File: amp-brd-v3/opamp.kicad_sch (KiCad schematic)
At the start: 21 parts, among them U2 INA233, U4 LMR36510ADDA

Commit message: Tested DAC and INA, doing new boards
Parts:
- added R8, R9: 10k, Resistor_SMD:R_0402_1005Metric, symbol Device:R
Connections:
- net SCL: now also R9.1
- net SDA: now also R8.1
- net V_{BUS}: now also R8.2, R9.2
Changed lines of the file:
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@@
+	)
+	(junction
+		(at 242.57 106.68)
+		(diameter 0)
+		(color 0 0 0 0)
+	)
+	(junction
+		(at 245.11 109.22)
+		(diameter 0)
+		(color 0 0 0 0)
 	)
 	(junction
@@
 	)
 	(junction
+		(at 242.57 81.28)
+		(diameter 0)
+		(color 0 0 0 0)
+	)
+	(junction
 		(at 57.15 147.32)
 		(diameter 0)
@@
 	(wire
 		(pts
+			(xy 245.11 95.25) (xy 245.11 109.22)
+		)
+		(stroke
+			(width 0)
+			(type default)
+		)
+	)
+	(wire
+		(pts
 			(xy 97.79 135.89) (xy 100.33 135.89)
 		)
@@
 	(wire
 		(pts
+			(xy 245.11 109.22) (xy 250.19 109.22)
+		)
+		(stroke
+			(width 0)
+			(type default)
+		)
+	)
+	(wire
+		(pts
 			(xy 45.72 134.62) (xy 45.72 147.32)
 		)
@@
 	(wire
 		(pts
+			(xy 242.57 81.28) (xy 245.11 81.28)
+		)
+		(stroke
+			(width 0)
+			(type default)
+		)
+	)
+	(wire
+		(pts
 			(xy 139.7 118.11) (xy 130.81 118.11)
 		)
@@
 	(wire
 		(pts
+			(xy 242.57 81.28) (xy 242.57 87.63)
+		)
+		(stroke
+			(width 0)
+			(type default)
+		)
+	)
+	(wire
+		(pts
+			(xy 245.11 81.28) (xy 245.11 87.63)
+		)
+		(stroke
+			(width 0)
+			(type default)
+		)
+	)
+	(wire
+		(pts
 			(xy 209.55 67.31) (xy 215.9 67.31)
 		)
@@
 	(wire
 		(pts
+			(xy 242.57 106.68) (xy 250.19 106.68)
+		)
+		(stroke
+			(width 0)
+			(type default)
+		)
+	)
+	(wire
+		(pts
+			(xy 242.57 95.25) (xy 242.57 106.68)
+		)
+		(stroke
+			(width 0)
+			(type default)
+		)
+	)
+	(wire
+		(pts
 			(xy 83.82 125.73) (xy 96.52 125.73)
 		)
@@
 	(wire
 		(pts
-			(xy 226.06 109.22) (xy 250.19 109.22)
+			(xy 226.06 109.22) (xy 245.11 109.22)
 		)
 		(stroke
@@
 	(wire
 		(pts
-			(xy 226.06 106.68) (xy 250.19 106.68)
+			(xy 226.06 106.68) (xy 242.57 106.68)
 		)
 		(stroke
@@
 		(pts
 			(xy 119.38 118.11) (xy 119.38 120.65)
+		)
+		(stroke
+			(width 0)
+			(type default)
+		)
+	)
+	(wire
+		(pts
+			(xy 237.49 81.28) (xy 242.57 81.28)
 		)
 		(stroke
@@
 		(shape input)
 		(at 85.09 135.89 180)
+		(effects
+			(font
+				(size 1.27 1.27)
+			)
+			(justify right)
+		)
+	)
+	(hierarchical_label "V_{BUS}"
+		(shape input)
+		(at 237.49 81.28 180)
 		(effects
 			(font
@@
 	)
 	(symbol
+		(lib_id "Device:R")
+		(at 242.57 91.44 180)
+		(unit 1)
+		(exclude_from_sim no)
+		(in_bom yes)
+		(on_board yes)
+		(dnp no)
+		(property "Reference" "R8"
+			(at 238.506 90.17 0)
+			(effects
+				(font
+					(size 1.27 1.27)
+				)
+				(justify right)
+			)
+		)
+		(property "Value" "10k"
+			(at 242.57 93.218 90)
+			(effects
+				(font
+					(size 1.27 1.27)
+				)
+				(justify right)
+			)
+		)
+		(property "Footprint" "Resistor_SMD:R_0402_1005Metric"
+			(at 244.348 91.44 90)
+			(effects
+				(font
+					(size 1.27 1.27)
+				)
+				(hide yes)
+			)
+		)
+		(property "Datasheet" "~"
+			(at 242.57 91.44 0)
+			(effects
+				(font
+					(size 1.27 1.27)
+				)
+				(hide yes)
+			)
+		)
+		(property "Description" "Resistor"
+			(at 242.57 91.44 0)
+			(effects
+				(font
+					(size 1.27 1.27)
+				)
+				(hide yes)
+			)
+		)
+		(pin "2"
+		)
+		(pin "1"
+		)
+		(instances
+			(project "amplifier-brd"
+				(path "/4a199ccc-be1f-4132-9551-a46e36599bcb/f2b7aa34-9911-40d3-beee-632deab3d3cc"
+					(reference "R8")
+					(unit 1)
+				)
+			)
+		)
+	)
+	(symbol
 		(lib_id "Device:C")
 		(at 34.29 130.81 0)
@@
 					(unit 1)
 				)
+			)
+		)
+	)
+	(symbol
+		(lib_id "Device:R")
+		(at 245.11 91.44 180)
+		(unit 1)
+		(exclude_from_sim no)
+		(in_bom yes)
+		(on_board yes)
+		(dnp no)
+		(property "Reference" "R9"
+			(at 246.634 90.17 0)
+			(effects
+				(font
+					(size 1.27 1.27)
+				)
+				(justify right)
+			)
+		)
+		(property "Value" "10k"
+			(at 245.11 93.218 90)
+			(effects
+				(font
+					(size 1.27 1.27)
+				)
+				(justify right)
+			)
+		)
+		(property "Footprint" "Resistor_SMD:R_0402_1005Metric"
+			(at 246.888 91.44 90)
+			(effects
+				(font
+					(size 1.27 1.27)
+				)
+				(hide yes)
+			)
+		)
+		(property "Datasheet" "~"
+			(at 245.11 91.44 0)
+			(effects
+				(font
+					(size 1.27 1.27)
+				)
+				(hide yes)
+			)
+		)
+		(property "Description" "Resistor"
+			(at 245.11 91.44 0)
+			(effects
+				(font
+					(size 1.27 1.27)
+				)
+				(hide yes)
+			)
+		)
+		(pin "2"
+		)
+		(pin "1"
+		)
+		(instances
+			(project "amplifier-brd"
+				(path "/4a199ccc-be1f-4132-9551-a46e36599bcb/f2b7aa34-9911-40d3-beee-632deab3d3cc"
+					(reference "R9")
+					(unit 1)
+				)

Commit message: Updated all boards for production
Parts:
- R3: value 10k -> 100k
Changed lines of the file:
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@@
 		)
 	)
-	(text_box "V_{OUT} = -A V_{CTRL} + (1 + A) V_{FB}\nA = R1 / R2\n\nV_{FB} = 1 V\nV_{OUT,absmin} = 1 V\nV_{OUT,absmax} = 28V\n\nR1 = 100k\nR2 = 4.02k\nA = 24.8756\n\nV_{OUT,max} = 25.8756 V\nV_{IN,absmin} = V_{OUT,max} / 0.95 = 27.24 V\nV_{CTRL,min} = 0 ==> V_{OUT} = V_{OUT,max} = 25.8765 V\n\nR_{LOAD} = 20 Ohm\nV_{CTRL,max} = 1.0 V  ==> V_{OUT} = V_{OUT,absmin} = 1.0 V, P_{OUT,absmin} = 0.05 W\nV_{CTRL,max} = 0.96 V ==> V_{OUT} = 2 V, P_{OUT} = 0.2 W\n"
+	(text_box "V_{OUT} = -A V_{CTRL} + (1 + A) V_{FB}\nA = R1 / R2\n\nV_{FB} = 1 V\nV_{OUT,absmin} = 1 V\nV_{OUT,absmax} = 28V\n\nR1 = 100k\nR2 = 4.02k\nA = 24.8756\n\nV_{OUT,max} = 25.8756 V\nV_{IN,absmin} = V_{OUT,max} / 0.95 = 27.24 V\nV_{CTRL,min} = 0 ==> V_{OUT} = V_{OUT,max} = 25.8765 V\n\nR_{LOAD} = 20 Ohm\nV_{CTRL,max} = 1.0 V  ==> V_{OUT} = V_{OUT,absmin} = 1.0 V, P_{OUT,absmin} = 0.05 W\nV_{CTRL,max} = 0.96 V ==> V_{OUT} = 2 V, P_{OUT} = 0.2 W\n\nCTRL_{IN} = High-Z => V_{FB} = 1V = V_{OUT} * 104k / 204k => V_{OUT} = 204 V / 104 ~ 1.96 V\n"
 		(exclude_from_sim no)
 		(at 13.97 13.97 0)
@@
 		(on_board yes)
 		(dnp no)
-		(fields_autoplaced yes)
 		(property "Reference" "R3"
-			(at 115.57 138.43 90)
-			(effects
-				(font
-					(size 1.27 1.27)
-				)
-			)
-		)
-		(property "Value" "10k"
-			(at 115.57 140.97 90)
-			(effects
-				(font
+			(at 120.904 144.78 90)
+			(effects
+				(font
+					(size 1.27 1.27)
+				)
+			)
+		)
+		(property "Value" "100k"
+			(at 115.57 144.78 90)
+			(effects
+				(font

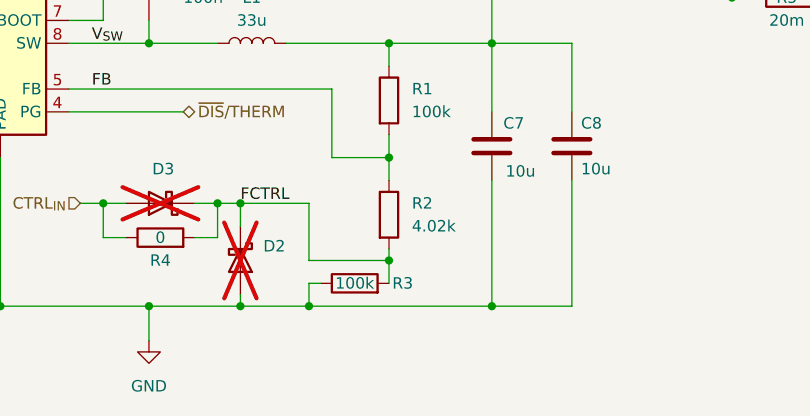
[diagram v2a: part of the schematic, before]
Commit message: Added part numbers
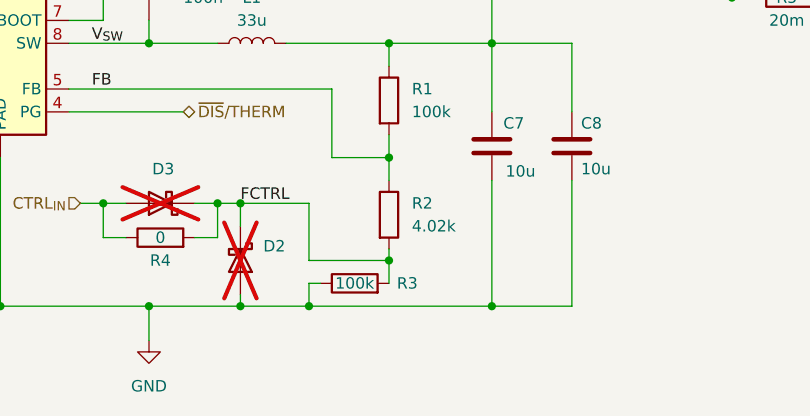
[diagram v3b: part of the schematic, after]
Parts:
- C1, D2, D3, R1, R2: Package (none) -> 0402
- C2, C4, R5: Package (none) -> 0805
- C6, C9: Package (none) -> 0603
- C7, C8: Package (none) -> 1210
- L1: Package (none) -> SMD
- R3: Mfr (none) -> Vishay-Dale; Mfr # (none) -> CRCW0402100KFKED; Package (none) -> 0402
- R4: Mfr (none) -> Walsin; Mfr # (none) -> MR04X0000FTL; Package (none) -> 0402
- R8, R9: Mfr (none) -> TE Connectivity / Holsworthy; Mfr # (none) -> RP73PF1E10KBTD; Package (none) -> 0402
- U2: Mfr (none) -> Texas Instruments; Mfr # (none) -> INA233AIDGSR; Package (none) -> SMD
- U4: Mfr (none) -> Texas Instruments; Mfr # (none) -> LMR36510ADDAR; Package (none) -> SMD
